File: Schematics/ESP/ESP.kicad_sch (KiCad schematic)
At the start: 18 parts, among them J1 Barrel_Jack, Q5 IRLB8721PBF, Q6 IRLB8721PBF, SW2 SW_Push, U1 AP9101CK, U2 AP9101CK, U3 AP9101CK, U8 74LVC1G11, U9 74LVC1G11

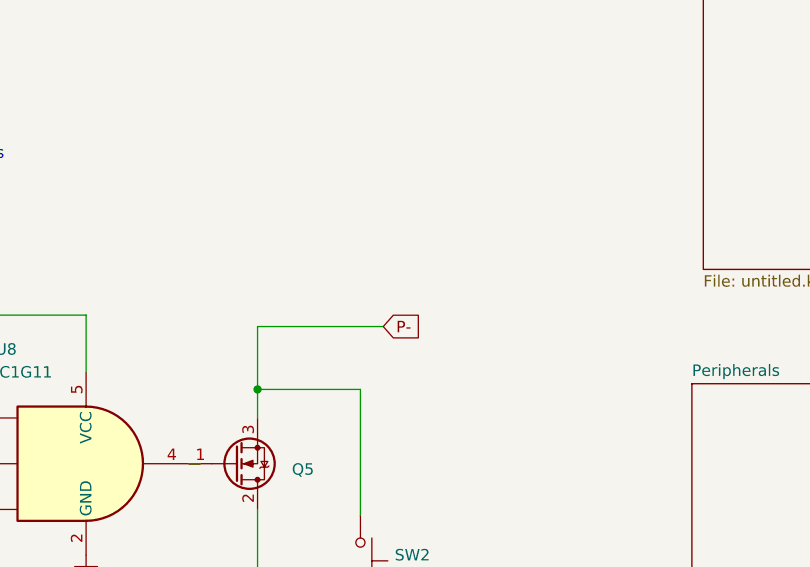
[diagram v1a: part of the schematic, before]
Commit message: PCB layout done no wiring
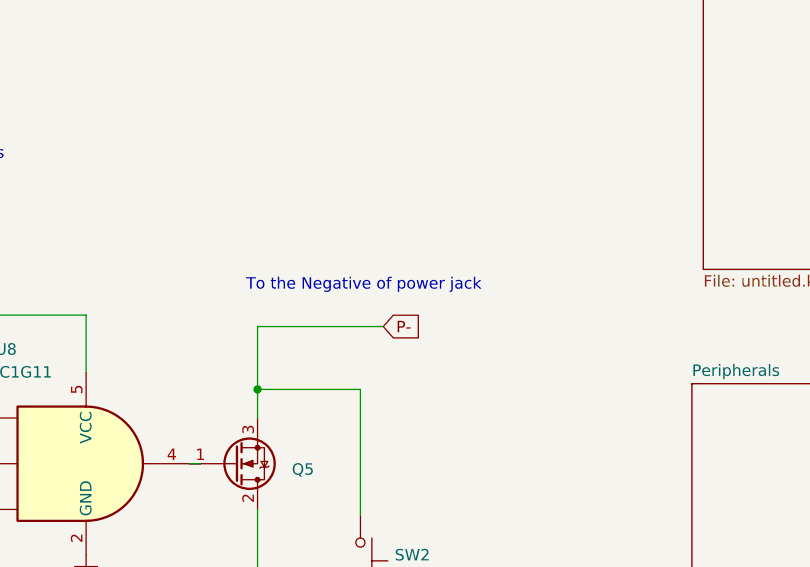
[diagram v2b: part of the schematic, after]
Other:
- note added: "To the Negative of power jack"
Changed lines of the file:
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@@
+    (effects (font (size 1.27 1.27)) (justify left bottom))
+  )
+  (text "To the Negative of power jack" (at 176.53 57.15 0)
     (effects (font (size 1.27 1.27)) (justify left bottom))
   )

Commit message: did some stuff
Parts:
- removed R11, R5, R9: 2.7k, Resistor_SMD:R_1206_3216Metric_Pad1.30x1.75mm_HandSolder, symbol Device:R
- removed R2, R3, R6: 330, Resistor_SMD:R_1206_3216Metric_Pad1.30x1.75mm_HandSolder, symbol Device:R
- removed U1, U2, U3: AP9101CK, Package_TO_SOT_SMD:SOT-23-5, symbol Battery_Management:AP9101CK
- removed U8, U9: 74LVC1G11, Package_TO_SOT_SMD:SOT-23-6_Handsoldering, symbol 74xGxx:74LVC1G11
- added C16, C17: 100nF, Capacitor_SMD:C_1206_3216Metric_Pad1.33x1.80mm_HandSolder, symbol Device:C_Small
- added C18: 1µF, Capacitor_SMD:C_1206_3216Metric_Pad1.33x1.80mm_HandSolder, symbol Device:C_Small
- added R11, R2, R5, R6, R9: 1k, symbol Device:R_Small
- added R24: 450K, symbol Device:R_Small
- added R3: 10k, symbol Device:R_Small
- added U1: BQ7791500PWT, SOP65P640X120-24N, symbol BQ7791500PWT:BQ7791500PWT
- C1: value 100nF -> 1µF
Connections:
- net Cell1+: now also R6.1; no longer C1.1
- net Cell2+: now also R5.1; no longer C2.1
- net GND: now also C1.2, C16.2, C17.2, C18.1, R3.2, U1.16 (CBI), U1.23 (CTRC), U1.24 (CTRD), U1.9 (VSS)
- net P-: now also R24.2
- net at C2.2: now also C3.1, R5.2, U1.6 (VC2)
- net at C3.2: now also C16.1, R6.2, U1.7 (VC1)
- net Battery+ renamed Cell3+
- net Cell3+: now also R11.2, R2.1
- net Battery-: no longer names the net of Q6.3 (S), SW2.2
- net Battery-: no longer C3.1
- new net: C1.1, R11.1, U1.1 (VDD)
- new net: R24.1, U1.14 (LD)
- new net: R3.1, U1.18 (TS)
- new net: C18.2, U1.2 (AVDD)
- new net: C2.1, R2.2, U1.5 (VC3)
- new net: C17.1, R9.2, U1.8 (VC0)
- new net Cell1-: R9.1
- no-connect marks 0 -> 3
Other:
- note removed: "CO/DO pins are high when battery voltage is within allowed range, thus a´ctivating their respective switches. when all the switches are activated, the final two MOSFETs are activated and the negative terminal of the battery is connected to the negative terminal of the circuit"
- note removed: "Capacitor and resistor to stabilize input voltage, recommeneded values are: 330 Ohm and 100nF"
- note removed: "current sense resistor, value recommended by datatsheet 2.7K"

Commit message: lots of stuff
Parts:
- removed SW2: SW_Push, Button_Switch_SMD:SW_SPST_PTS645, symbol Switch:SW_Push
- added C19: 100nF, Capacitor_SMD:C_1206_3216Metric_Pad1.33x1.80mm_HandSolder, symbol Device:C_Small
- added C20, C21: 1µF, Capacitor_SMD:C_1206_3216Metric_Pad1.33x1.80mm_HandSolder, symbol Device:C_Small
- added R25, R33: 1M, Resistor_SMD:R_1206_3216Metric_Pad1.30x1.75mm_HandSolder, symbol Device:R_Small
- added R26, R27: 100, Resistor_SMD:R_1206_3216Metric_Pad1.30x1.75mm_HandSolder, symbol Device:R_Small
- added R28: 100K, Resistor_SMD:R_1206_3216Metric_Pad1.30x1.75mm_HandSolder, symbol Device:R_Small
- added R29: 10K, Resistor_SMD:R_1206_3216Metric_Pad1.30x1.75mm_HandSolder, symbol Device:R_Small
- added R30: 3.3M, Resistor_SMD:R_1206_3216Metric_Pad1.30x1.75mm_HandSolder, symbol Device:R_Small
- added R31: 1k, Resistor_SMD:R_1206_3216Metric_Pad1.30x1.75mm_HandSolder, symbol Device:R_Small
- added R32: 4.5K, Resistor_SMD:R_1206_3216Metric_Pad1.30x1.75mm_HandSolder, symbol Device:R_Small
- R11, R2, R3, R5, R6, R9: footprint (none) -> Resistor_SMD:R_1206_3216Metric_Pad1.30x1.75mm_HandSolder; Price (none) -> 0,11; digikey link (none) -> https://www.digikey.fi/en/products/detail/yageo/RC1206FR-07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
- R24: footprint (none) -> Resistor_SMD:R_1206_3216Metric_Pad1.30x1.75mm_HandSolder; Price (none) -> 0.11; digikey link (none) -> https://www.digikey.fi/en/products/detail/yageo/RC1206FR-07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
- U1: Price (none) -> 2.52; digikey link (none) -> https://www.digikey.fi/en/products/detail/texas-instruments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
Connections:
- net Cell1- is gone; now on net GND: R9.1
- net GND: now also U1.20 (CCFG), C20.2, C21.2, R25.2, R27.2, R28.2
- net P-: now also R30.1
- net at C1.1, R11.1, U1.1 (VDD): now also R29.1
- net at U1.10 (SRP): now also C19.2, C21.1, R27.1
- net at U1.11 (SRN): now also C19.1, C20.1, R26.1
- net DSG: now reaches U1.12 (DSG)
- net DSG: now also R32.2
- net CHG: now reaches U1.13 (CHG)
- net CHG: now also R31.2
- net at U1.17 (OCDP): now also R28.1
- net at U1.22 (PRES): now also R29.2
- net at U1.3 (VC5): now also C2.1, R2.2, U1.4 (VC4), U1.5 (VC3)
- net at Q5.1 (G): now also R30.2, R31.1
- net at Q6.1 (G): now also R32.1, R33.2
- net at Q6.3 (S): now also R25.1, R26.2, R33.1
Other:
- note removed: "Important note: To kickstart the circuit, the negative battery terminal needs to be shorted to the negative charger terminal using this switch"
- note removed: "To the Negative of power jack"
- moved on the sheet: Q5, Q6, R11, R24, U1

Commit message: added esp32 connected
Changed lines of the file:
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@@
   (junction (at 50.8 85.725) (diameter 0) (color 0 0 0 0)
+  )
+  (junction (at 116.84 64.77) (diameter 0) (color 0 0 0 0)
+  )
+  (junction (at 116.205 120.65) (diameter 0) (color 0 0 0 0)
   )
   (junction (at 161.925 92.075) (diameter 0) (color 0 0 0 0)
@@
     (stroke (width 0) (type default))
   )
+  (wire (pts (xy 116.84 64.77) (xy 121.285 64.77))
+    (stroke (width 0) (type default))
+  )
   (wire (pts (xy 126.365 85.09) (xy 114.3 85.09))
     (stroke (width 0) (type default))
@@
     (stroke (width 0) (type default))
   )
-  (wire (pts (xy 78.105 115.57) (xy 78.74 115.57))
-    (stroke (width 0) (type default))
-  )
   (wire (pts (xy 114.3 87.63) (xy 126.365 87.63))
     (stroke (width 0) (type default))
@@
     (stroke (width 0) (type default))
   )
-  (wire (pts (xy 116.205 120.65) (xy 114.3 120.65))
-    (stroke (width 0) (type default))
-  )
-  (wire (pts (xy 114.3 64.77) (xy 121.285 64.77))
+  (wire (pts (xy 114.3 64.77) (xy 116.84 64.77))
     (stroke (width 0) (type default))
   )
@@
     (stroke (width 0) (type default))
   )
+  (wire (pts (xy 116.84 120.65) (xy 116.205 120.65))
+    (stroke (width 0) (type default))
+  )
   (wire (pts (xy 50.8 79.375) (xy 46.355 79.375))
     (stroke (width 0) (type default))
@@
     (stroke (width 0) (type default))
   )
+  (wire (pts (xy 114.3 120.65) (xy 116.205 120.65))
+    (stroke (width 0) (type default))
+  )
   (wire (pts (xy 126.365 80.645) (xy 126.365 85.09))
     (stroke (width 0) (type default))
@@
   )
   (wire (pts (xy 72.39 90.17) (xy 72.39 92.71))
+    (stroke (width 0) (type default))
+  )
+  (wire (pts (xy 116.84 62.23) (xy 116.84 64.77))
     (stroke (width 0) (type default))
   )
@@
     )
   )
+  (symbol (lib_id "power:PWR_FLAG") (at 116.84 62.23 0) (unit 1)
+    (in_bom yes) (on_board yes) (dnp no) (fields_autoplaced)
+    (property "Reference" "#FLG05" (at 116.84 60.325 0)
+      (effects (font (size 1.27 1.27)) hide)
+    )
+    (property "Value" "PWR_FLAG" (at 116.84 59.055 0)
+      (effects (font (size 1.27 1.27)))
+    )
+    (property "Footprint" "" (at 116.84 62.23 0)
+      (effects (font (size 1.27 1.27)) hide)
+    )
+    (property "Datasheet" "~" (at 116.84 62.23 0)
+      (effects (font (size 1.27 1.27)) hide)
+    )
+    (pin "1")
+    (instances
+      (project "ESP"
+        (path "/b616d203-cf5c-462f-b907-860a8573592a/9ad1e8da-d13f-4a6e-8aa2-8655a1d493de"
+          (reference "#FLG05") (unit 1)
+        )
+        (path "/b616d203-cf5c-462f-b907-860a8573592a"
+          (reference "#FLG03") (unit 1)
+        )
+      )
+    )
+  )
   (symbol (lib_id "power:GND") (at 134.62 72.39 0) (unit 1)
     (in_bom yes) (on_board yes) (dnp no) (fields_autoplaced)
@@
         )
       )
+    )
+  )
+  (symbol (lib_id "power:PWR_FLAG") (at 116.84 120.65 270) (unit 1)
+    (in_bom yes) (on_board yes) (dnp no) (fields_autoplaced)
+    (property "Reference" "#FLG05" (at 118.745 120.65 0)
+      (effects (font (size 1.27 1.27)) hide)
+    )
+    (property "Value" "PWR_FLAG" (at 120.65 121.285 90)
+      (effects (font (size 1.27 1.27)) (justify left))
+    )
+    (property "Footprint" "" (at 116.84 120.65 0)
+      (effects (font (size 1.27 1.27)) hide)
+    )
+    (property "Datasheet" "~" (at 116.84 120.65 0)
+      (effects (font (size 1.27 1.27)) hide)
+    )
+    (pin "1")
+    (instances
+      (project "ESP"
+        (path "/b616d203-cf5c-462f-b907-860a8573592a/9ad1e8da-d13f-4a6e-8aa2-8655a1d493de"
+          (reference "#FLG05") (unit 1)
+        )
+        (path "/b616d203-cf5c-462f-b907-860a8573592a"
+          (reference "#FLG04") (unit 1)
+        )
+      )

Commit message: fixed bom
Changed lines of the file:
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@@
   (junction (at 116.84 64.77) (diameter 0) (color 0 0 0 0)
   )
-  (junction (at 116.205 120.65) (diameter 0) (color 0 0 0 0)
-  )
   (junction (at 161.925 92.075) (diameter 0) (color 0 0 0 0)
   )
@@
   )
   (junction (at 134.62 64.77) (diameter 0) (color 0 0 0 0)
-  )
-  (junction (at 38.735 79.375) (diameter 0) (color 0 0 0 0)
   )
   (junction (at 50.8 104.775) (diameter 0) (color 0 0 0 0)
@@
     (stroke (width 0) (type default))
   )
-  (wire (pts (xy 116.84 120.65) (xy 116.205 120.65))
-    (stroke (width 0) (type default))
-  )
   (wire (pts (xy 50.8 79.375) (xy 46.355 79.375))
     (stroke (width 0) (type default))
   )
   (wire (pts (xy 175.26 71.12) (xy 175.26 64.135))
-    (stroke (width 0) (type default))
-  )
-  (wire (pts (xy 37.465 79.375) (xy 38.735 79.375))
     (stroke (width 0) (type default))
   )
@@
     (effects (font (size 1.27 1.27)) (justify left))
     (property "Intersheetrefs" "${INTERSHEET_REFS}" (at 161.925 28.5418 90)
-      (effects (font (size 1.27 1.27)) (justify right) hide)
-    )
-  )
-  (global_label "Cell1-" (shape input) (at 37.465 79.375 180) (fields_autoplaced)
-    (effects (font (size 1.27 1.27)) (justify right))
-    (property "Intersheetrefs" "${INTERSHEET_REFS}" (at 28.0883 79.375 0)
       (effects (font (size 1.27 1.27)) (justify right) hide)
     )
@@
         )
       )
-    )
-  )
-  (symbol (lib_id "power:PWR_FLAG") (at 116.84 120.65 270) (unit 1)
-    (in_bom yes) (on_board yes) (dnp no) (fields_autoplaced)
-    (property "Reference" "#FLG05" (at 118.745 120.65 0)
-      (effects (font (size 1.27 1.27)) hide)
-    )
-    (property "Value" "PWR_FLAG" (at 120.65 121.285 90)
-      (effects (font (size 1.27 1.27)) (justify left))
-    )
-    (property "Footprint" "" (at 116.84 120.65 0)
-      (effects (font (size 1.27 1.27)) hide)
-    )
-    (property "Datasheet" "~" (at 116.84 120.65 0)
-      (effects (font (size 1.27 1.27)) hide)
-    )
-    (pin "1")
-    (instances
-      (project "ESP"
-        (path "/b616d203-cf5c-462f-b907-860a8573592a/9ad1e8da-d13f-4a6e-8aa2-8655a1d493de"
-          (reference "#FLG05") (unit 1)
-        )
-        (path "/b616d203-cf5c-462f-b907-860a8573592a"
-          (reference "#FLG04") (unit 1)
-        )
-      )
